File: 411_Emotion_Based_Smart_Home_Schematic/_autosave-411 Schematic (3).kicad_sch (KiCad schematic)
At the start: 24 parts, among them Q1 NSS1C301ET4G, Q2 NSS1C301ET4G, Q3 NSS1C301ET4G, U4 HC-SR04

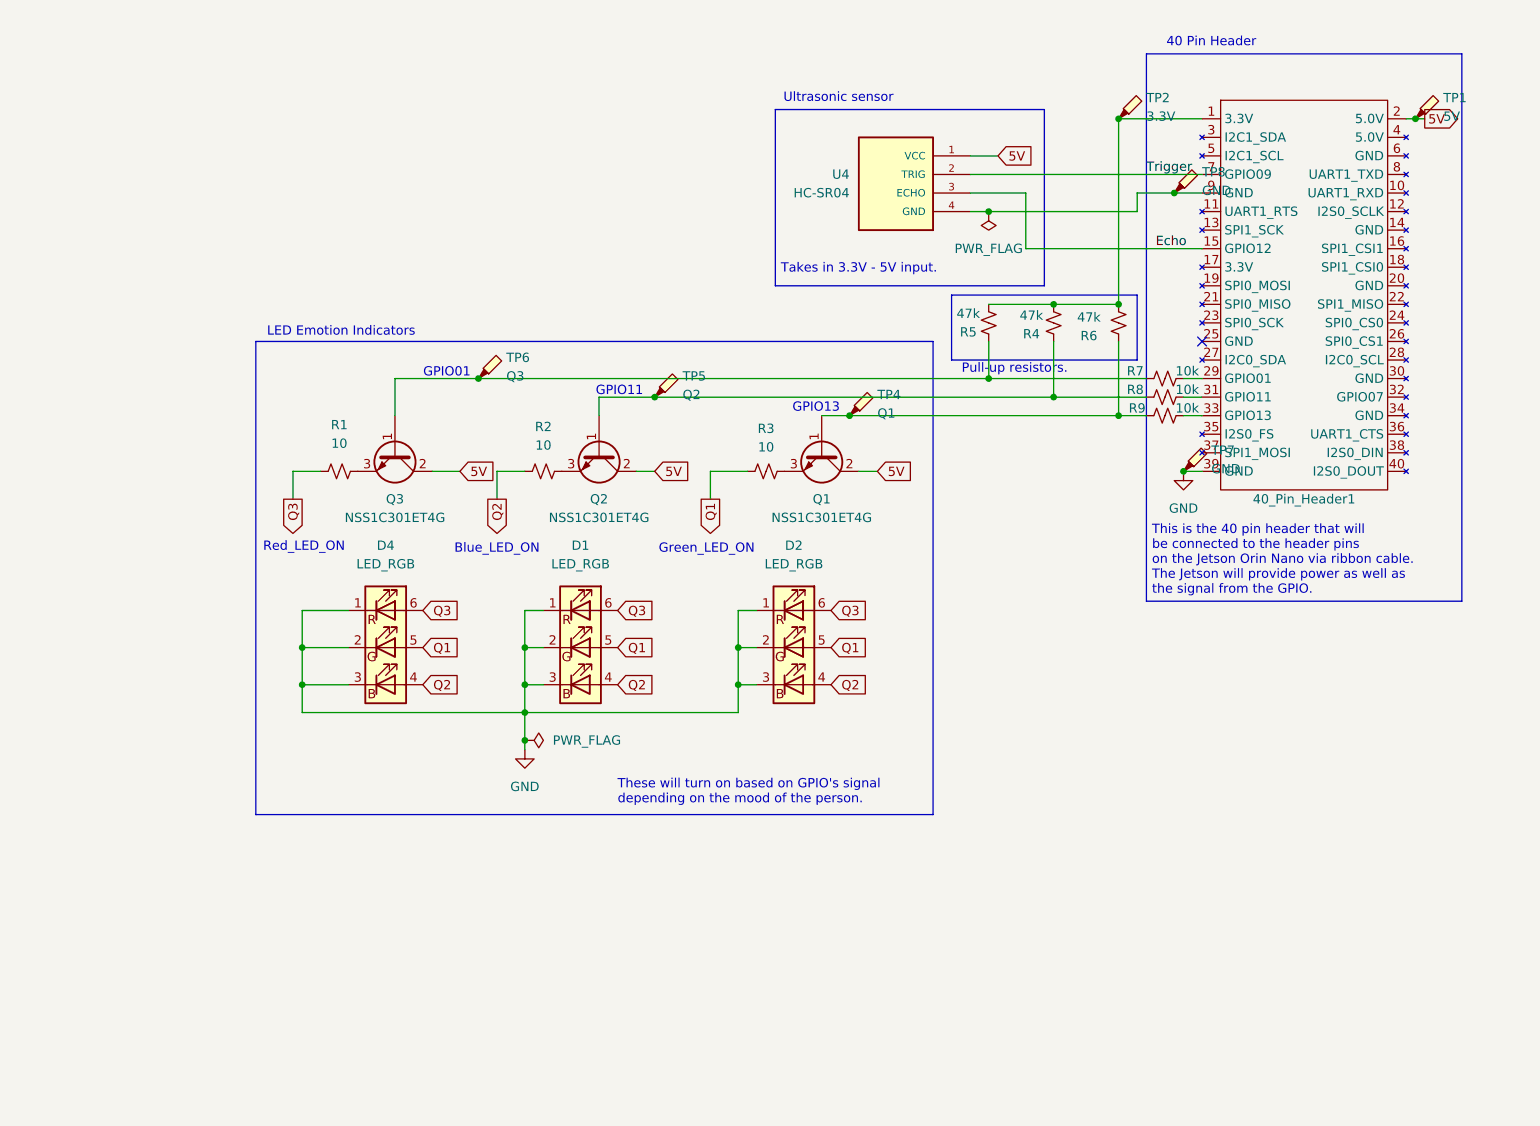
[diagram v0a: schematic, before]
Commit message: Updated schematic.
Added limiting resistors to each GPIO pins.
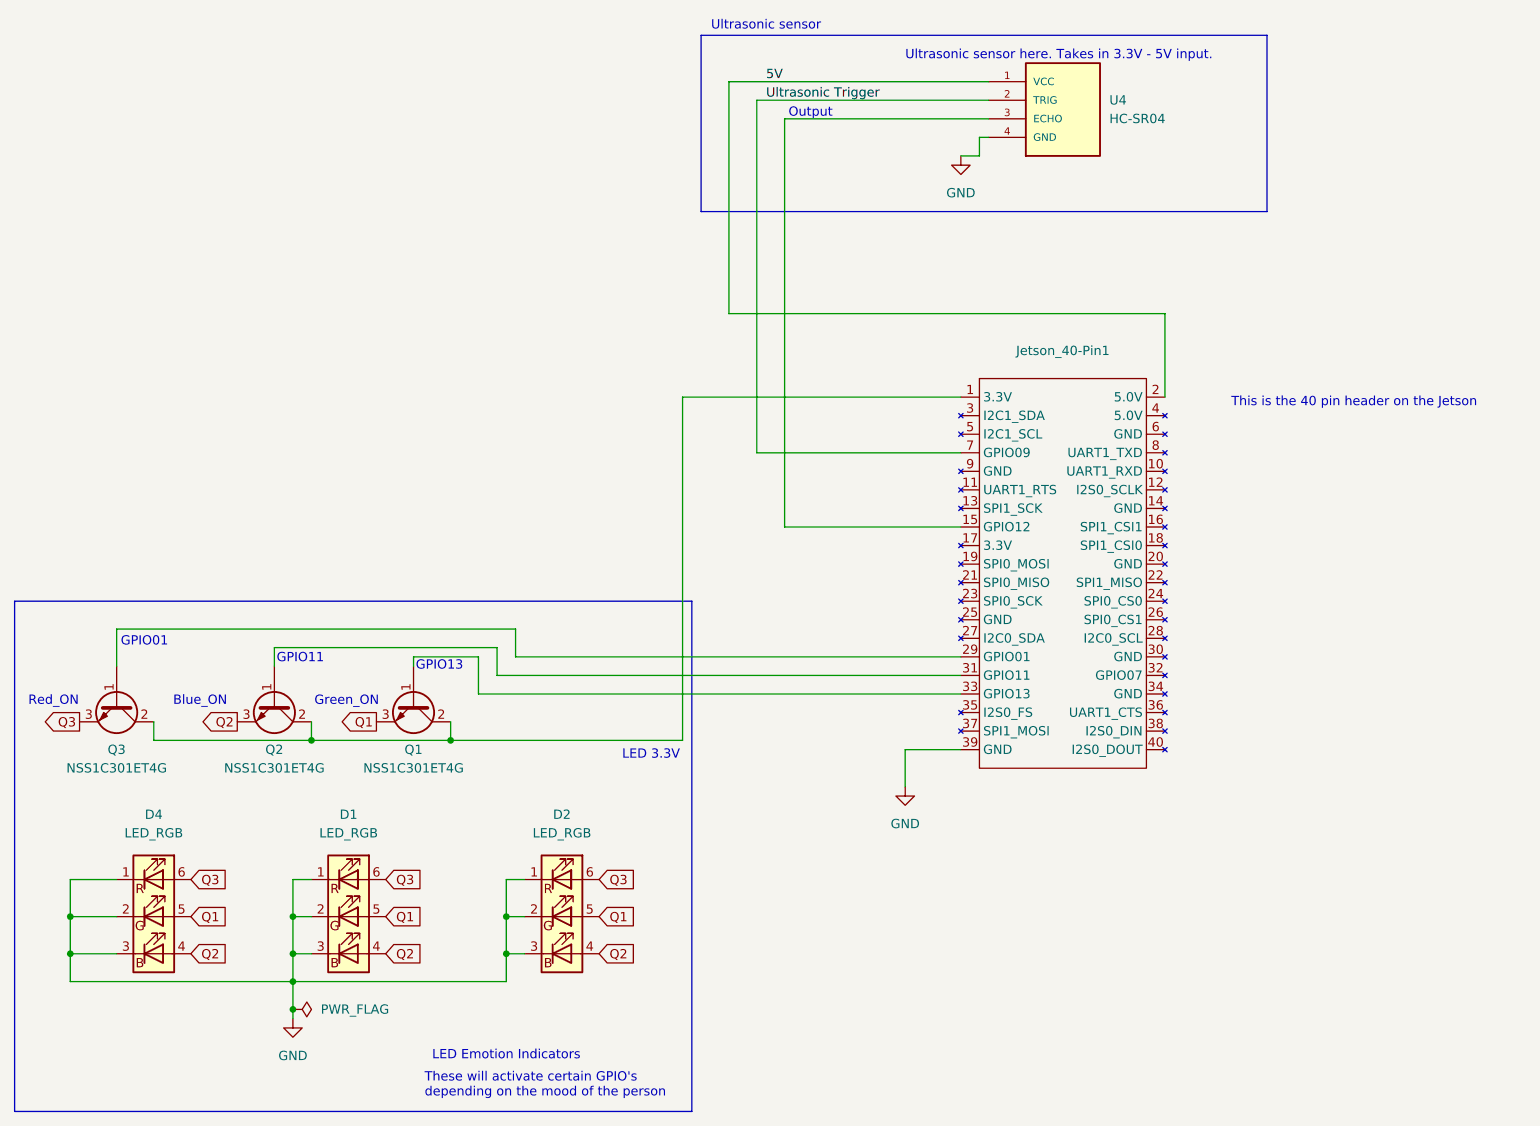
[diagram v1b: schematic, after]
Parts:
- removed R1, R2, R3: 10, Resistor_THT:R_Axial_DIN0411_L9.9mm_D3.6mm_P5.08mm_Vertical, symbol Device:R_Small_US
- removed R4, R5, R6: 47k, Resistor_THT:R_Axial_DIN0411_L9.9mm_D3.6mm_P5.08mm_Vertical, symbol Device:R_Small_US
- removed R7, R8, R9: 10k, Resistor_THT:R_Axial_DIN0411_L9.9mm_D3.6mm_P5.08mm_Vertical, symbol Device:R_Small_US
- removed TP1: 5V, TestPoint:TestPoint_Pad_1.0x1.0mm, symbol Connector:TestPoint_Probe
- removed TP2: 3.3V, TestPoint:TestPoint_Pad_1.0x1.0mm, symbol Connector:TestPoint_Probe
- removed TP4: Q1, TestPoint:TestPoint_Pad_1.0x1.0mm, symbol Connector:TestPoint_Probe
- removed TP5: Q2, TestPoint:TestPoint_Pad_1.0x1.0mm, symbol Connector:TestPoint_Probe
- removed TP6: Q3, TestPoint:TestPoint_Pad_1.0x1.0mm, symbol Connector:TestPoint_Probe
- removed TP7, TP8: GND, TestPoint:TestPoint_Pad_1.0x1.0mm, symbol Connector:TestPoint_Probe
- renumbered 40_Pin_Header1 to Jetson_40-Pin1
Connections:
- net 5V: no longer Q1.2 (C), Q2.2 (C), Q3.2 (C)
- net GND: now also U4.4 (GND)
- net Q1: now also Q1.3 (E)
- net Q2: now also Q2.3 (E)
- net Q3: now also Q3.3 (E)
- net at Jetson_40-Pin1.1 (3.3V): now also Q1.2 (C), Q2.2 (C), Q3.2 (C)
- net at Jetson_40-Pin1.29 (GPIO01): now also Q3.1 (B)
- net at Jetson_40-Pin1.31 (GPIO11): now also Q2.1 (B)
- net at Jetson_40-Pin1.33 (GPIO13): now also Q1.1 (B)
- net at Jetson_40-Pin1.9 (GND): no longer U4.4 (GND)
- net Echo: no longer names the net of Jetson_40-Pin1.15 (GPIO12), U4.3 (ECHO)
- net Trigger renamed Ultrasonic Trigger
- no-connect marks 1 -> 0
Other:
- note added: "Blue_ON"
- note added: "Green_ON"
- note added: "LED 3.3V"
- note added: "Output"
- note added: "Red_ON"
- note added: "These will activate certain GPIO's depending on the mood of the person"
- note added: "This is the 40 pin header on the Jetson"
- note added: "Ultrasonic sensor here. Takes in 3.3V - 5V input."
- note removed: "40 Pin Header"
- note removed: "Blue_LED_ON"
- note removed: "Green_LED_ON"
- note removed: "Pull-up resistors."
- note removed: "Red_LED_ON"
- note removed: "Takes in 3.3V - 5V input."
- note removed: "These will turn on based on GPIO's signal depending on the mood of the person."
- note removed: "This is the 40 pin header that will be connected to the header pins on the Jetson Orin Nano via ribbon cable. The Jetson will provide power as well as the signal from the GPIO."
- moved on the sheet: D1, D2, D4, Q1, Q2, Q3, U4
